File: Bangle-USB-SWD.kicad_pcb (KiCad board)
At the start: 2 copper layers, 37.6 x 21.4 mm, 3 parts, among them J1 USB_A, J2 Conn_02x05_Odd_Even, J3 Conn_01x02_Male

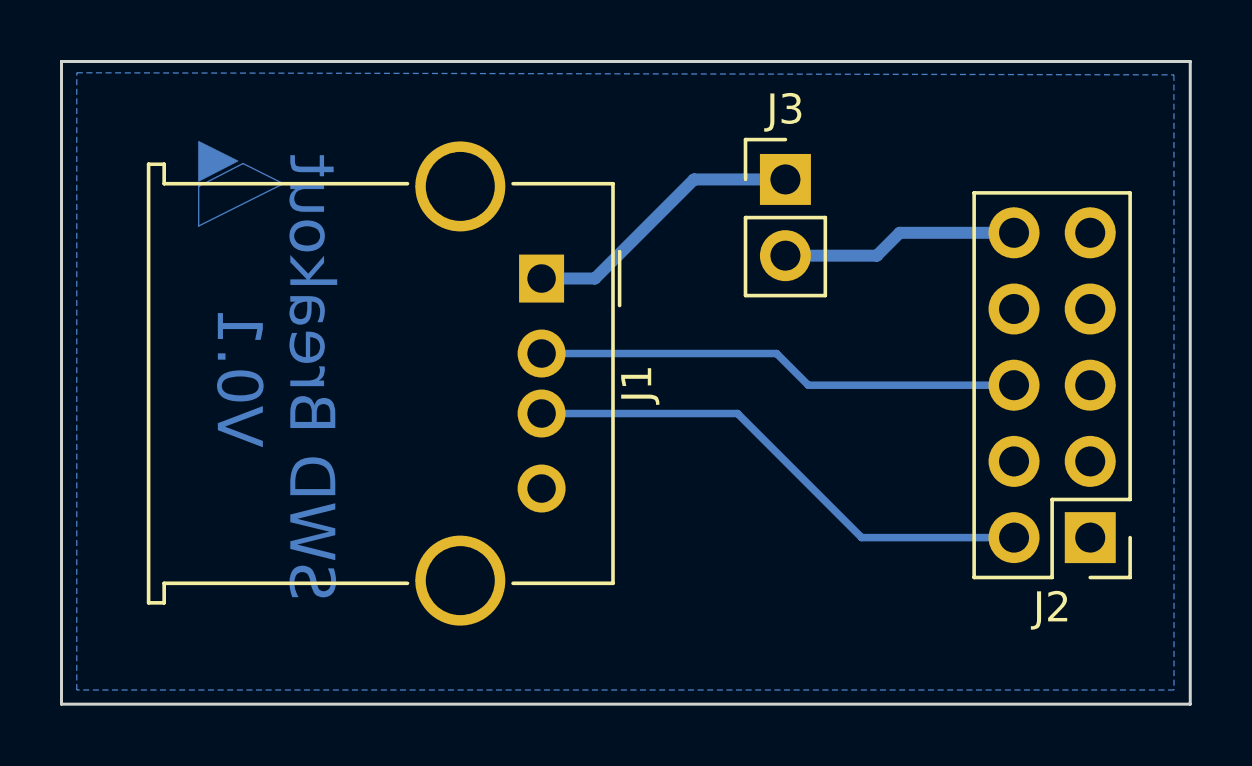
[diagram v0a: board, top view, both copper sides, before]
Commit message: oops, SWDIO nd SWCLK swapped on USB type-A conntector, fixed
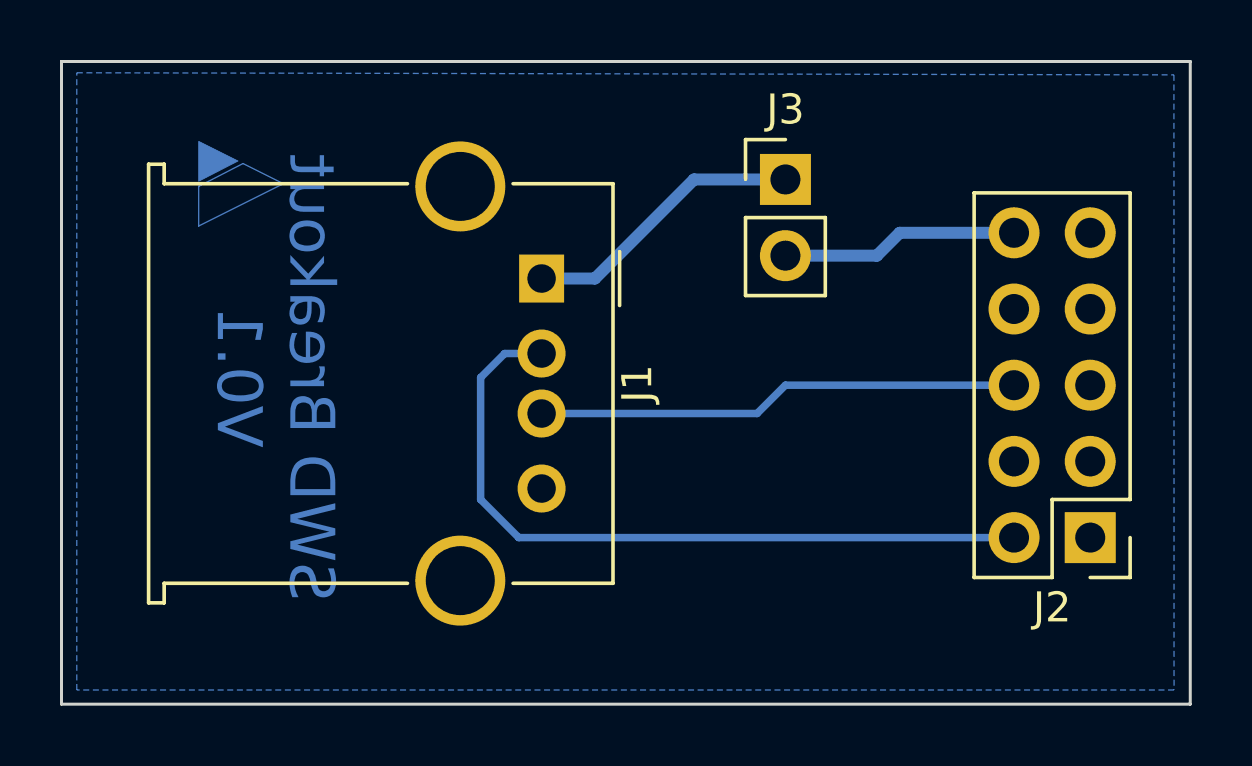
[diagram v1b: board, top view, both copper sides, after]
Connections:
- J1 pad 2: /SWCLK -> /SWD
- J1 pad 3: /SWD -> /SWCLK
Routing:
- net /SWD: track 17.5 -> 24.7 mm
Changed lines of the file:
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@@
       (net 5 "/Vbus") (pinfunction "VBUS") (pintype "power_in"))
     (pad "2" thru_hole circle (at 2.5 0 270) (size 1.6 1.6) (drill 0.95) (layers *.Cu *.Mask)
-      (net 6 "/SWCLK") (pinfunction "D-") (pintype "bidirectional"))
+      (net 7 "/SWD") (pinfunction "D-") (pintype "bidirectional"))
     (pad "3" thru_hole circle (at 4.5 0 270) (size 1.6 1.6) (drill 0.95) (layers *.Cu *.Mask)
-      (net 7 "/SWD") (pinfunction "D+") (pintype "bidirectional"))
+      (net 6 "/SWCLK") (pinfunction "D+") (pintype "bidirectional"))
     (pad "4" thru_hole circle (at 7 0 270) (size 1.6 1.6) (drill 0.95) (layers *.Cu *.Mask)
       (net 4 "/GND") (pinfunction "GND") (pintype "power_in"))
@@
   (segment (start 88.9 76.454) (end 92.202 73.152) (width 0.4) (layer "B.Cu") (net 5))
   (segment (start 92.202 73.152) (end 95.25 73.152) (width 0.4) (layer "B.Cu") (net 5))
-  (segment (start 96.012 80.01) (end 94.956 78.954) (width 0.25) (layer "B.Cu") (net 6))
-  (segment (start 102.87 80.01) (end 96.012 80.01) (width 0.25) (layer "B.Cu") (net 6))
-  (segment (start 94.956 78.954) (end 87.122 78.954) (width 0.25) (layer "B.Cu") (net 6))
-  (segment (start 87.122 80.954) (end 93.654 80.954) (width 0.25) (layer "B.Cu") (net 7))
-  (segment (start 93.654 80.954) (end 97.79 85.09) (width 0.25) (layer "B.Cu") (net 7))
-  (segment (start 97.79 85.09) (end 102.87 85.09) (width 0.25) (layer "B.Cu") (net 7))
+  (segment (start 94.306 80.954) (end 95.25 80.01) (width 0.25) (layer "B.Cu") (net 6))
+  (segment (start 87.122 80.954) (end 94.306 80.954) (width 0.25) (layer "B.Cu") (net 6))
+  (segment (start 95.25 80.01) (end 102.87 80.01) (width 0.25) (layer "B.Cu") (net 6))
+  (segment (start 87.122 78.954) (end 85.892 78.954) (width 0.25) (layer "B.Cu") (net 7))
+  (segment (start 86.36 85.09) (end 102.87 85.09) (width 0.25) (layer "B.Cu") (net 7))
+  (segment (start 85.892 78.954) (end 85.09 79.756) (width 0.25) (layer "B.Cu") (net 7))
+  (segment (start 85.09 83.82) (end 86.36 85.09) (width 0.25) (layer "B.Cu") (net 7))
+  (segment (start 85.09 79.756) (end 85.09 83.82) (width 0.25) (layer "B.Cu") (net 7))
   (segment (start 99.06 74.93) (end 102.87 74.93) (width 0.4) (layer "B.Cu") (net 10))
   (segment (start 95.25 75.692) (end 98.298 75.692) (width 0.4) (layer "B.Cu") (net 10))

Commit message: fix logo, add 'made in', recreate 3D views
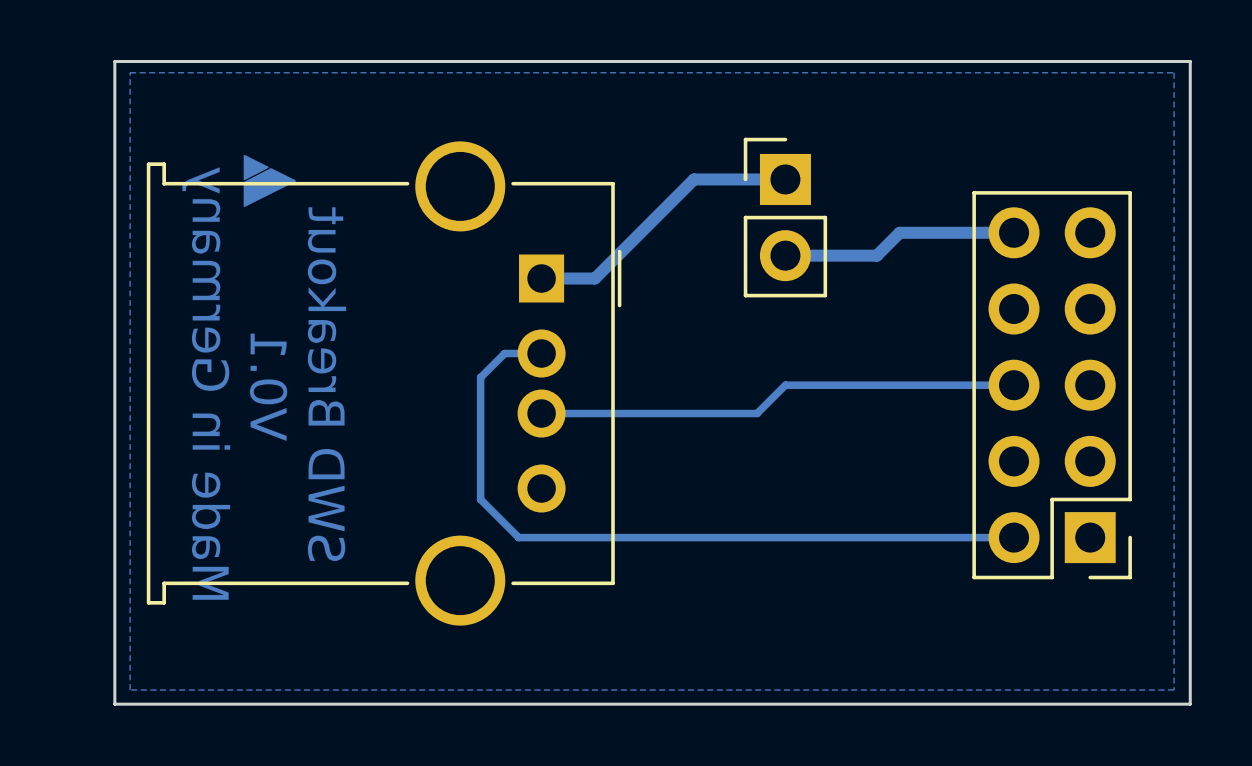
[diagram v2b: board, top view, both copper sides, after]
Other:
- board size 37.6 x 21.4 mm -> 35.8 x 21.4 mm
- board text added: "SWD Breakout V0.1 Made in Germany"
- board text removed: "SWD Breakout V0.1"
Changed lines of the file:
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@@
     (property "Sheetname" "")
     (attr through_hole)
-    (fp_text reference "J2" (at 1.27 -2.33) (layer "F.SilkS")
-      (effects (font (size 1 1) (thickness 0.15)))
-    )
-    (fp_text value "Conn_02x05_Odd_Even" (at 1.27 12.49) (layer "F.Fab")
-      (effects (font (size 1 1) (thickness 0.15)))
-    )
-    (fp_text user "${REFERENCE}" (at 1.27 5.08 90) (layer "F.Fab")
+    (fp_text reference "J2" (at -7.62 7.366) (layer "F.SilkS") hide
+      (effects (font (size 1 1) (thickness 0.15)))
+    )
+    (fp_text value "Conn_02x05_Odd_Even" (at -15.24 11.43) (layer "F.Fab") hide
+      (effects (font (size 1 1) (thickness 0.15)))
+    )
+    (fp_text user "${REFERENCE}" (at -12.192 6.858 90) (layer "F.Fab") hide
       (effects (font (size 1 1) (thickness 0.15)))
     )
@@
     (property "Sheetname" "")
     (attr through_hole)
-    (fp_text reference "J1" (at 3.5 -3.19 90) (layer "F.SilkS")
-      (effects (font (size 1 1) (thickness 0.15)))
-    )
-    (fp_text value "USB_A" (at 3.5 14.5 90) (layer "F.Fab")
-      (effects (font (size 1 1) (thickness 0.15)))
-    )
-    (fp_text user "${REFERENCE}" (at 3.5 3.7 90) (layer "F.Fab")
+    (fp_text reference "J1" (at 2.794 17.272 90) (layer "F.SilkS") hide
+      (effects (font (size 1 1) (thickness 0.15)))
+    )
+    (fp_text value "USB_A" (at -0.762 17.272 90) (layer "F.Fab") hide
+      (effects (font (size 1 1) (thickness 0.15)))
+    )
+    (fp_text user "${REFERENCE}" (at 4.826 17.526 90) (layer "F.Fab") hide
       (effects (font (size 1 1) (thickness 0.15)))
     )
@@
     (property "Sheetname" "")
     (attr through_hole)
-    (fp_text reference "J3" (at 0 -2.33) (layer "F.SilkS")
-      (effects (font (size 1 1) (thickness 0.15)))
-    )
-    (fp_text value "Conn_01x02_Male" (at 0 4.87) (layer "F.Fab")
-      (effects (font (size 1 1) (thickness 0.15)))
-    )
-    (fp_text user "${REFERENCE}" (at 0 1.27 90) (layer "F.Fab")
+    (fp_text reference "J3" (at 20.066 4.572) (layer "F.SilkS") hide
+      (effects (font (size 1 1) (thickness 0.15)))
+    )
+    (fp_text value "Conn_01x02_Male" (at 23.622 2.54) (layer "F.Fab") hide
+      (effects (font (size 1 1) (thickness 0.15)))
+    )
+    (fp_text user "${REFERENCE}" (at -25.654 -0.762 90) (layer "F.Fab") hide
       (effects (font (size 1 1) (thickness 0.15)))
     )
@@
     )
   )
-  (gr_line (start 75.692 74.704222) (end 75.692 74.704222) (layer "B.Cu") (width 0.028222))
-  (gr_line (start 75.692 74.704222) (end 75.692 73.382705) (layer "B.Cu") (width 0.028222))
-  (gr_line (start 75.692 73.382705) (end 75.692 73.382705) (layer "B.Cu") (width 0.028222))
-  (gr_line (start 77.170352 72.621176) (end 78.514222 73.293111) (layer "B.Cu") (width 0.028222))
-  (gr_line (start 78.514222 73.293111) (end 75.692 74.704222) (layer "B.Cu") (width 0.028222))
-  (gr_line (start 75.692 73.382705) (end 77.170352 72.621176) (layer "B.Cu") (width 0.028222))
   (gr_poly
     (pts
-      (xy 77.002149 72.537074)
-      (xy 75.692 73.211653)
-      (xy 75.692 71.882)
-      (xy 77.002149 72.537074)
-    ) (layer "B.Cu") (width 0.028222) (fill solid))
-  (gr_rect (start 71.118856 69.220058) (end 108.744486 90.642392) (layer "Edge.Cuts") (width 0.1) (fill none))
-  (gr_text "SWD Breakout\nV0.1" (at 78.232 79.756 270) (layer "B.Cu")
-    (effects (font (size 1.5 1.5) (thickness 0.3)) (justify mirror))
+      (xy 78.002089 72.747253)
+      (xy 77.216 73.152)
+      (xy 77.216 72.354208)
+      (xy 78.002089 72.747253)
+    ) (layer "B.Cu") (width 0.047624) (fill solid))
+  (gr_poly
+    (pts
+      (xy 78.909333 73.200875)
+      (xy 77.216 74.047541)
+      (xy 77.216 73.254631)
+      (xy 78.103011 72.797714)
+      (xy 78.909333 73.200875)
+    ) (layer "B.Cu") (width 0.047624) (fill solid))
+  (gr_rect (start 72.896856 69.220058) (end 108.744486 90.642392) (layer "Edge.Cuts") (width 0.1) (fill none))
+  (gr_text "SWD Breakout\nV0.1\nMade in Germany" (at 77.978 80.01 270) (layer "B.Cu")
+    (effects (font (size 1.2 1.2) (thickness 0.1)) (justify mirror))
   )
   (segment (start 87.122 76.454) (end 88.9 76.454) (width 0.4) (layer "B.Cu") (net 5))
@@
       (pts
         (xy 108.204 90.17)
-        (xy 71.628 90.17)
-        (xy 71.628 69.596)
-        (xy 108.199924 69.66623)
+        (xy 73.406 90.17)
+        (xy 73.406 69.596)
+        (xy 108.204 69.596)
       )
     )
   )
-  (group "" (id 8892e406-375f-4b37-8253-f5a691eb6c8b)
+  (group "" (id d28b9bef-5584-45f3-ba80-1d1413db94cd)
     (members
-      25cd7335-f2dc-42c9-9825-0d06c3aba198
-      37551a27-1809-4d2d-9650-dcd17f577fc2
-      4e05d889-415f-4831-b4e1-0c1a80884d73
-      674c3318-506a-4fe3-a507-d3dbf0010ffc
-      abae5534-9994-4499-848f-f26c2063b80e
-      ddd6d888-35ac-4ccf-b282-be46bf0dc724
-      ff289e5f-3d8c-47bf-8897-ae964ebf1244
-    )
-  )
+      284ecb32-72bc-4d4a-b4d0-eff8e036d9c0
+      e3f9c19d-49ed-4e40-96fc-024c31789b7e
+    )
+  )
